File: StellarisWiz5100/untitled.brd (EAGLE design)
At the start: 97.5 x 61 mm, 5 parts

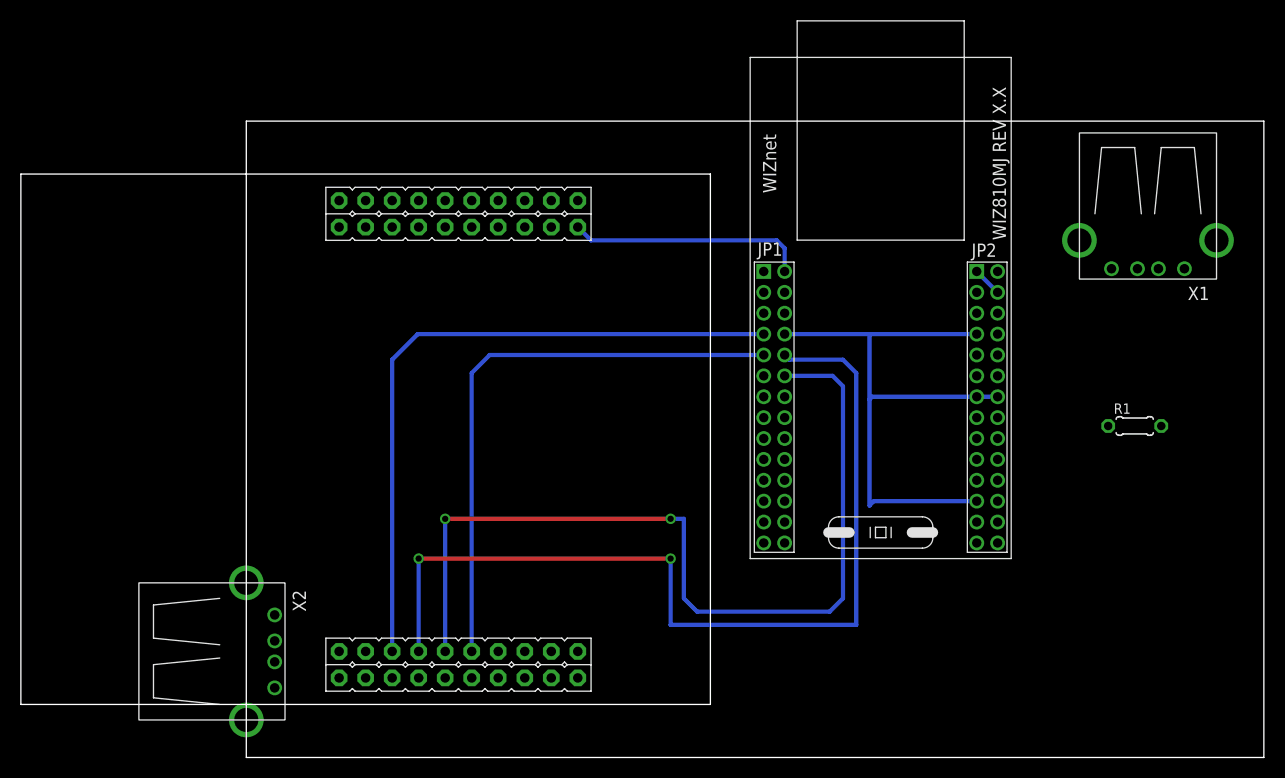
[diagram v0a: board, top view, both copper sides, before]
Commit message: 
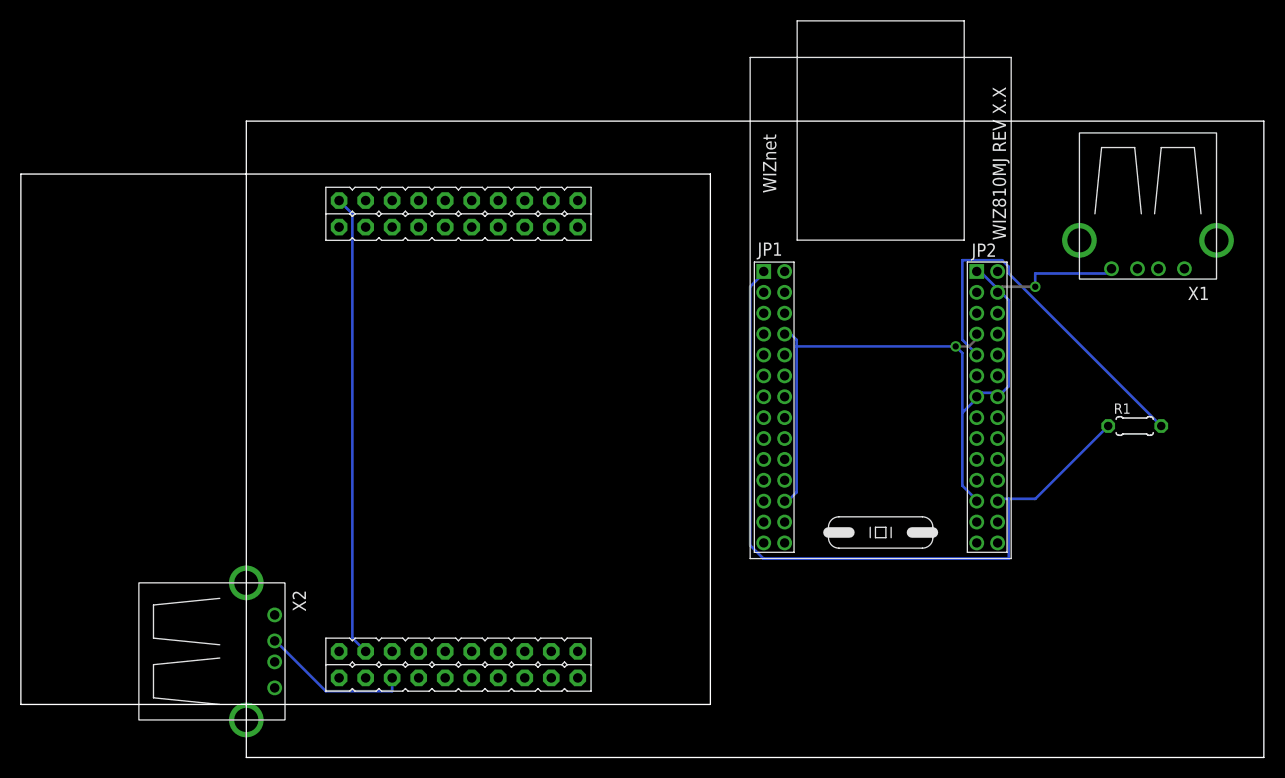
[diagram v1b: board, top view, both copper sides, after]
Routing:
- net N$5: track 88.9 -> 0.00 mm, vias 2 -> 0
- net N$4: track 85.8 -> 0.00 mm, vias 2 -> 0
- net VCC: track 0.00 -> 71.3 mm
- net GND: track 60.5 -> 126.4 mm, vias 0 -> 2
- net N$1: track 64.5 -> 0.00 mm
- net N$3: track 55.4 -> 0.00 mm
- net N$2: track 0.00 -> 35.6 mm
- net N$6: track 22.9 -> 0.00 mm
- net N$9: track 0.00 -> 14.5 mm
